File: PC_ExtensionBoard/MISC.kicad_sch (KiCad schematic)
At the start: 60 parts, among them J2 Conn_01x04_Pin, J3 Conn_01x16_MountingPin, Q7 BSS138-7-F, Q8 BSS138-7-F, U37 9DBL0651CKILF, U38 74AUP2G132, U4 STM32G0B1RCT6, Y1 Oscillator_32.768kHz_ECS_2520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

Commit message: update LCSC Number
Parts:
- removed J2: Conn_01x04_Pin, Connector_Hirose:Hirose_DF13-04P-1.25DSA_1x04_P1.25mm_Vertical, symbol Connector:Conn_01x04_Pin
- removed R182, R183, R184, R185: R_1k_0402, PC_Components_1:R_0402_1005Metric, symbol A_PC_ExtensionBoard:R_1k_0402
- added J6: Conn_01x04_Pin, Connector_PinSocket_2.00mm:PinSocket_1x04_P2.00mm_Vertical, symbol Connector:Conn_01x04_Pin
- added J7: Conn_01x02_Socket, symbol Connector:Conn_01x02_Socket
- added R196, R197, R198, R199: R_1k_0402, PC_Components_1:R_0402_1005Metric, symbol A_PC_ExtensionBoard:R_1k_0402
- added R246, R247, R248, R249: R_0R_0402, PC_Components_1:R_0402_1005Metric, symbol A_PC_ExtensionBoard:R_0R_0402
- R186, R187, R189, R190: Author Antmicro -> (none); LCSC (none) -> C202394; License Apache-2.0 -> (none); Manufacturer Bourns -> (none); Public False -> (none); Tolerance 1% -> (none)
- R193, R194, R195: LCSC (none) -> C242160
- U4: footprint PC_ExtensionBoard:LQFP-64_L10.0-W10.0-P0.50-LS12.0-BL -> Package_QFP:LQFP-64-1EP_10x10mm_P0.5mm_EP5x5mm; LCSC (none) -> C3034735
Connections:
- net +3.3V: now also R190.1; no longer R190.2
- net GND: now also J6.4 (Pin_4), R196.2, R197.2, R198.2, R199.2
- net MCU_SWCLK: now also J7.2 (Pin_2)
- net MCU_SWDIO: now also J7.1 (Pin_1)
- net at R178.2, U37.13 (~{OE0}): now also R199.1
- net at R316.2, U37.29 (~{OE3}): now also R196.1
- net at R315.2, U37.24 (~{OE2}): now also R197.1
- net at U37.40 (~{CKPWRGD_PD}): now also R190.2; no longer R190.1
- net at R314.2, U37.21 (~{OE1}): now also R198.1
- net at U4.1 (PC11): now also R248.1
- net at U4.2 (PC12): now also R249.1
- net at U4.49 (PC9): now also R246.1
- net at U4.64 (PC10): now also R247.1
- new net +12V: J6.3 (Pin_3)
- new net EN0: R246.2
- new net EN1: R247.2
- new net EN2: R248.2
- new net EN3: R249.2
- new net FAN.PWM: J6.1 (Pin_1)
- new net FAN.TACH: J6.2 (Pin_2)
- no-connect marks 8 -> 45

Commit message: update Schematic
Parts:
- added R84, R85: R_10k_0402, PC_Components_1:R_0402_1005Metric, symbol A_PC_ExtensionBoard:R_10k_0402
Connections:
- net GND: now also R85.2
- new net +3V3: R84.1
- new net SATA0-1_SATA_PCIE: R84.2, R85.1

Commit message: update diff pair routing
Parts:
- removed TP47, TP48: TP_0.75mm_SMD, PC_Components_1:TP_SMD_0.75mm, symbol A_PC_ExtensionBoard:TP_0.75mm_SMD
- J7: footprint (none) -> Connector_PinHeader_2.00mm:PinHeader_1x02_P2.00mm_Vertical
- R238, R239, R240, R241, R242, R243, R244, R245, R246, R247, R248, R249: now not fitted; now left out of the parts list
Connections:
- net ~{PWR_OK}: now also U4.54 (PD4)
- net DIF5+: no longer names the net of U37.36 (DIF5+)
- net DIF5-: no longer names the net of U37.37 (DIF5-)
- no-connect marks 45 -> 46

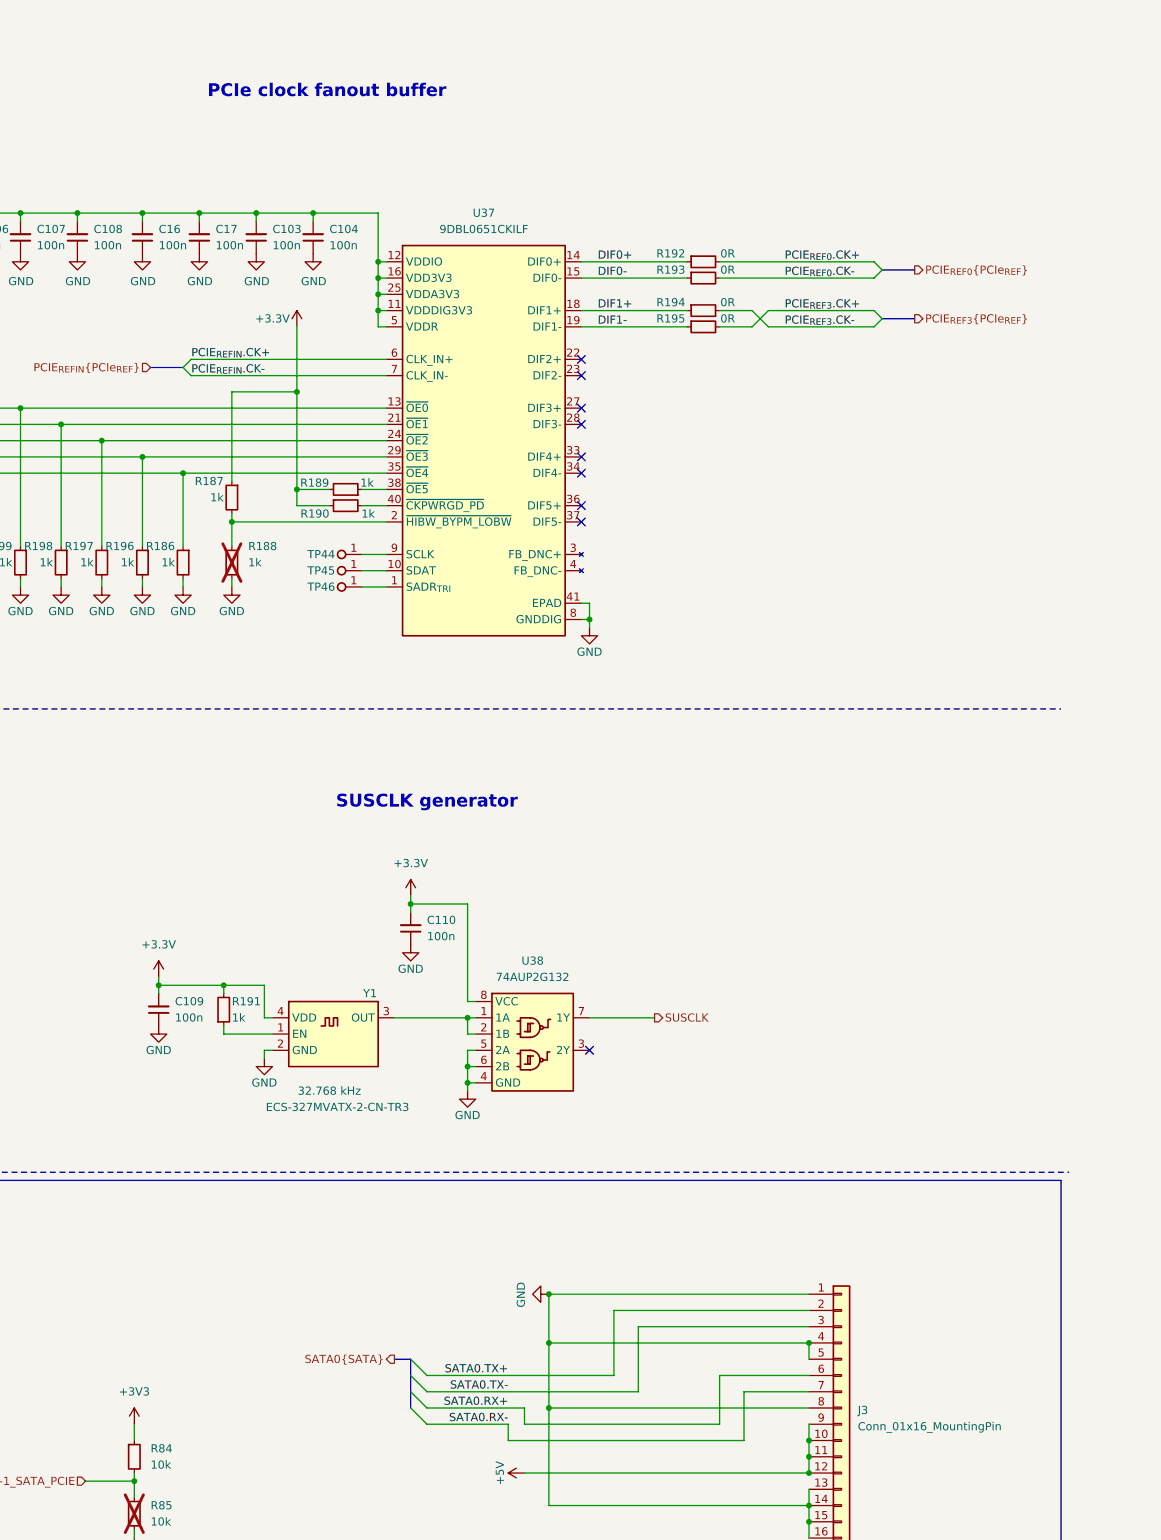
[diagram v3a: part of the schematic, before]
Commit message: attempts with impedance control
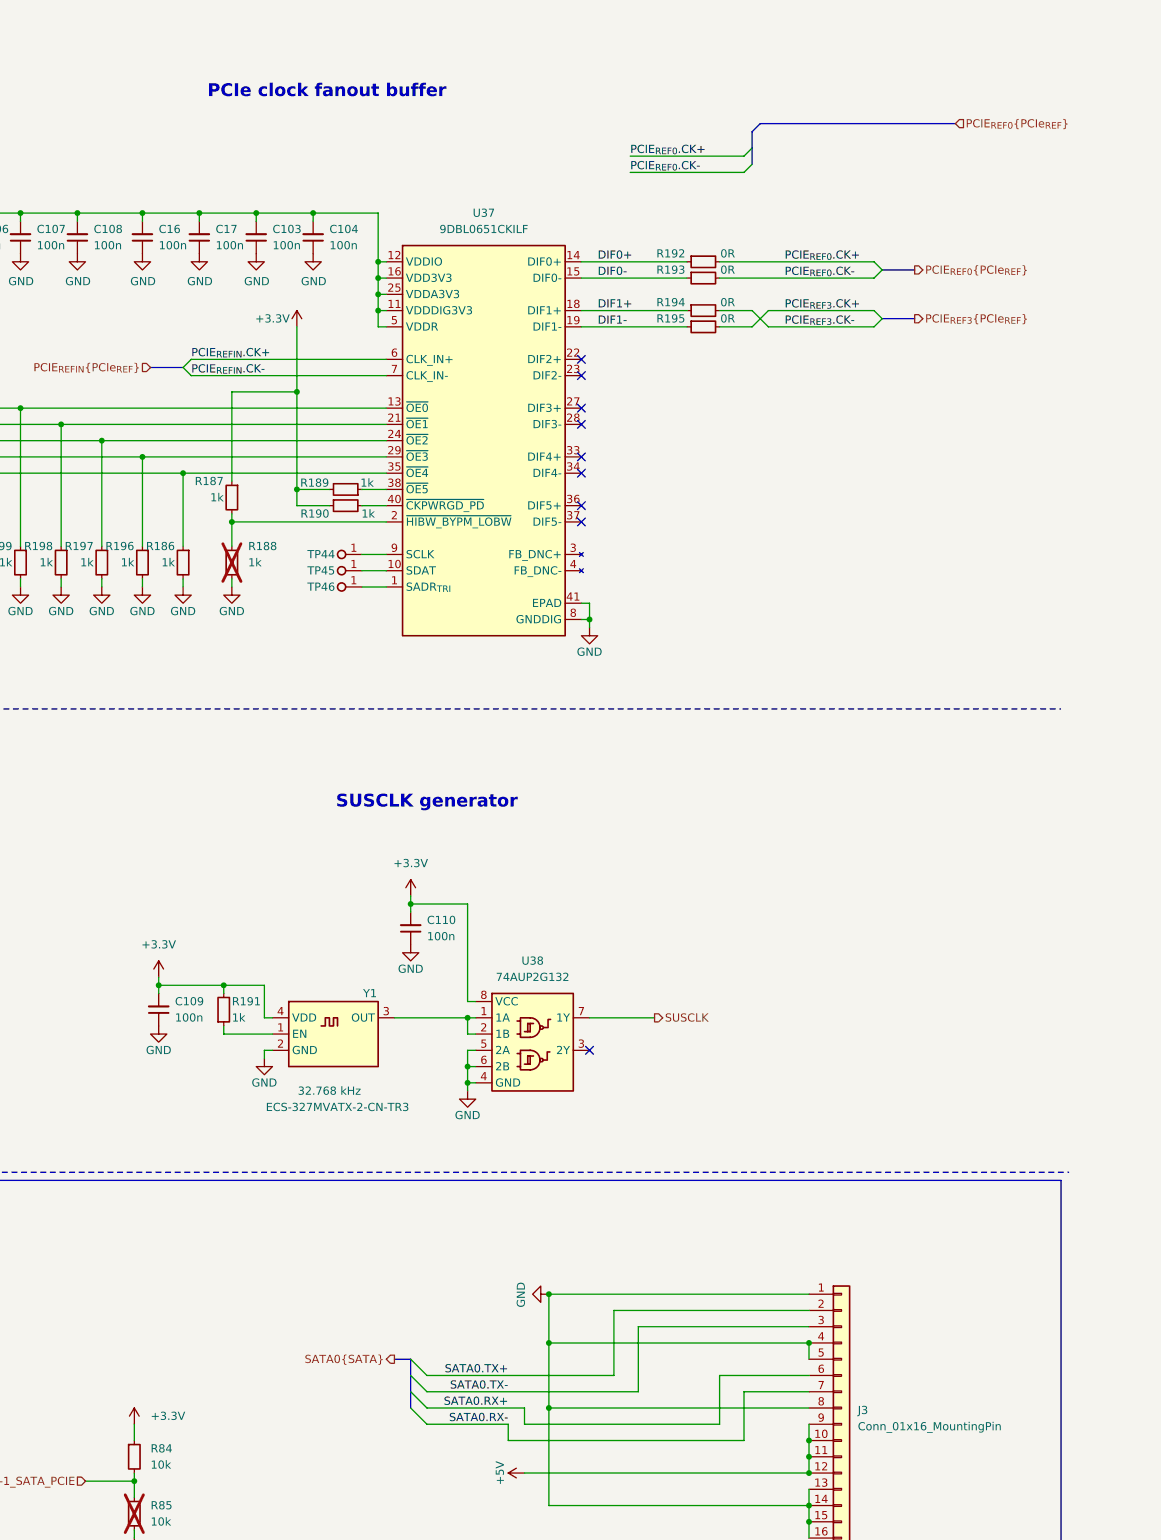
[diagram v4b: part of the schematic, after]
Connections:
- net +3V3 is gone; now on net +3.3V: R84.1
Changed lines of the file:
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@@
 	)
 	(bus_entry
+		(at 778.51 41.91)
+		(size 1.27 -1.27)
+		(stroke
+			(width 0)
+			(type default)
+		)
+	)
+	(bus_entry
 		(at 283.21 118.11)
 		(size 2.54 2.54)
@@
 	)
 	(bus_entry
+		(at 778.51 44.45)
+		(size 1.27 -1.27)
+		(stroke
+			(width 0)
+			(type default)
+		)
+	)
+	(bus_entry
 		(at 692.15 76.2)
 		(size -1.27 -1.27)
@@
 		)
 	)
+	(bus
+		(pts
+			(xy 781.05 36.83) (xy 811.53 36.83)
+		)
+		(stroke
+			(width 0)
+			(type default)
+		)
+	)
 	(wire
 		(pts
@@
 		)
 	)
+	(bus
+		(pts
+			(xy 779.78 40.64) (xy 779.78 38.1)
+		)
+		(stroke
+			(width 0)
+			(type default)
+		)
+	)
 	(wire
 		(pts
@@
 		)
 	)
+	(wire
+		(pts
+			(xy 760.73 44.45) (xy 778.51 44.45)
+		)
+		(stroke
+			(width 0)
+			(type default)
+		)
+	)
 	(polyline
 		(pts
@@
 	(wire
 		(pts
+			(xy 760.73 41.91) (xy 778.51 41.91)
+		)
+		(stroke
+			(width 0)
+			(type default)
+		)
+	)
+	(wire
+		(pts
 			(xy 704.85 181.61) (xy 703.58 181.61)
 		)
@@
 		)
 	)
+	(bus
+		(pts
+			(xy 779.78 38.1) (xy 781.05 36.83)
+		)
+		(stroke
+			(width 0)
+			(type default)
+		)
+	)
 	(wire
 		(pts
@@
 		)
 	)
+	(bus
+		(pts
+			(xy 779.78 43.18) (xy 779.78 40.64)
+		)
+		(stroke
+			(width 0)
+			(type default)
+		)
+	)
 	(wire
 		(pts
@@
 		)
 	)
+	(label "PCIE_{REF0}.CK+"
+		(at 760.73 41.91 0)
+		(effects
+			(font
+				(size 1.27 1.27)
+			)
+			(justify left bottom)
+		)
+	)
 	(label "LED_R"
 		(at 38.1 99.06 0)
@@
 	)
 	(label "PCIE_{REF0}.CK-"
+		(at 760.73 44.45 0)
+		(effects
+			(font
+				(size 1.27 1.27)
+			)
+			(justify left bottom)
+		)
+	)
+	(label "PCIE_{REF0}.CK-"
 		(at 784.86 60.96 0)
 		(effects
@@
 		)
 	)
+	(hierarchical_label "PCIE_{REF0}{PCIe_{REF}}"
+		(shape input)
+		(at 811.53 36.83 0)
+		(effects
+			(font
+				(size 1.27 1.27)
+			)
+			(justify left)
+		)
+	)
 	(hierarchical_label "GPIOEX6"
 		(shape output)
@@
 			)
 		)
-		(property "Value" "+3V3"
-			(at 683.26 234.95 0)
+		(property "Value" "+3.3V"
+			(at 685.8 238.7599 0)
 			(show_name no)
 			(do_not_autoplace no)
@@
 					(size 1.27 1.27)
 				)
+				(justify left)
 			)
 		)

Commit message: bug fixes
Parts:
- J6: LCSC C722763 -> (none)
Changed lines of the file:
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@@
-			)
-		)
-		(property "LCSC" "C722763"
-			(at 806.45 294.64 0)
-			(hide yes)
-			(show_name no)
-			(do_not_autoplace no)
-			(effects
-				(font
-					(size 1.27 1.27)
-				)
 			)
 		)

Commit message: bug fixes
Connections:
- net +3.3V: no longer C111.2, C112.2, C113.2, C114.2, U4.6 (VBAT), U4.8 (VDD)
- net PCIE_{REF0}.CK+ renamed PCIE_REF0.CK+
- net PCIE_{REF0}.CK- renamed PCIE_REF0.CK-
- net PCIE_{REF3}.CK+ renamed PCIE_REF3.CK+
- net PCIE_{REF3}.CK- renamed PCIE_REF3.CK-
- net PCIE_{REFIN}.CK+ renamed PCIE_REFIN.CK+
- net PCIE_{REFIN}.CK- renamed PCIE_REFIN.CK-
- new net +3V3_AON: C111.2, C112.2, C113.2, C114.2, U4.6 (VBAT), U4.8 (VDD)
